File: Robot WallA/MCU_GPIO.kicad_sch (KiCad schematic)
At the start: 2 parts, among them J13 10129383-916001ALF, J6 10129383-916001ALF

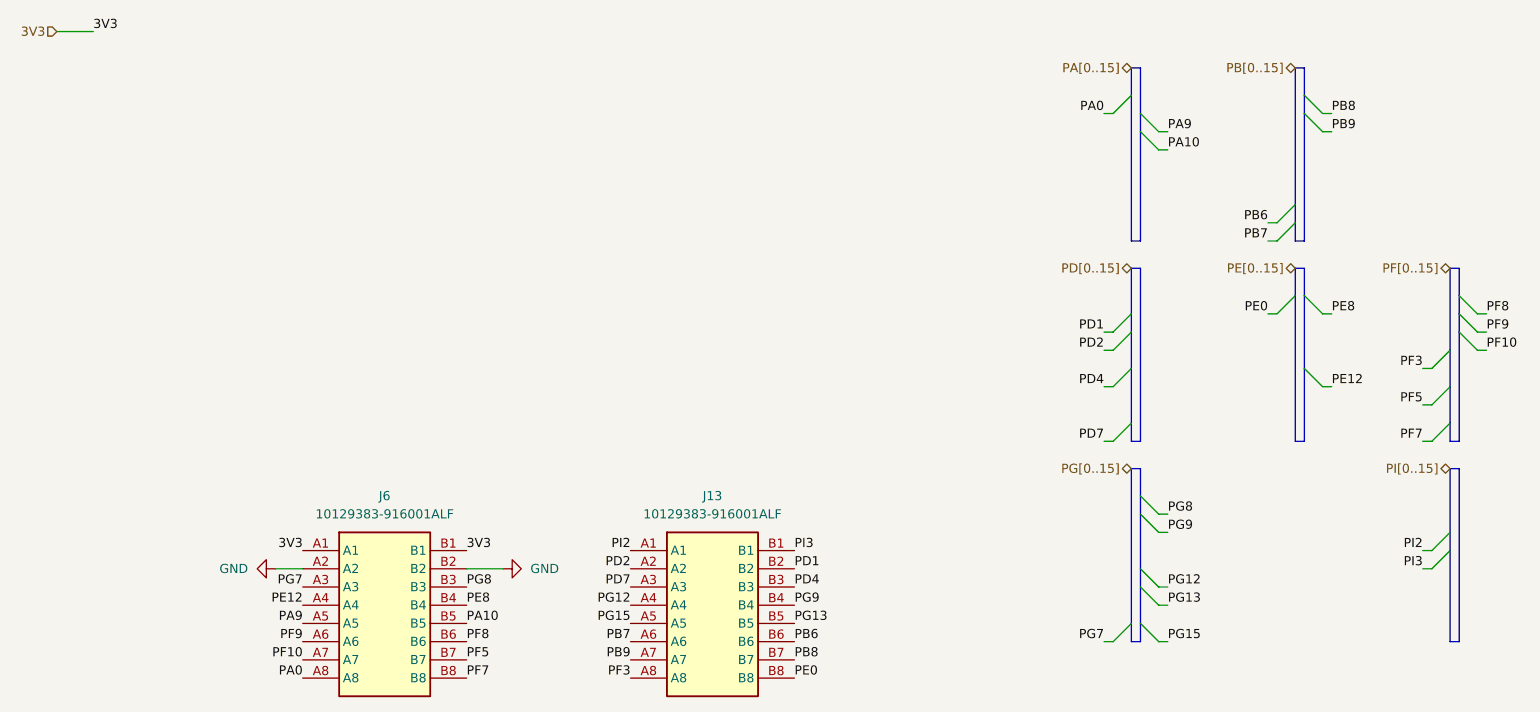
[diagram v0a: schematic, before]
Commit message: Modified a bit pin header pins to allow I2C,SPI and CAN
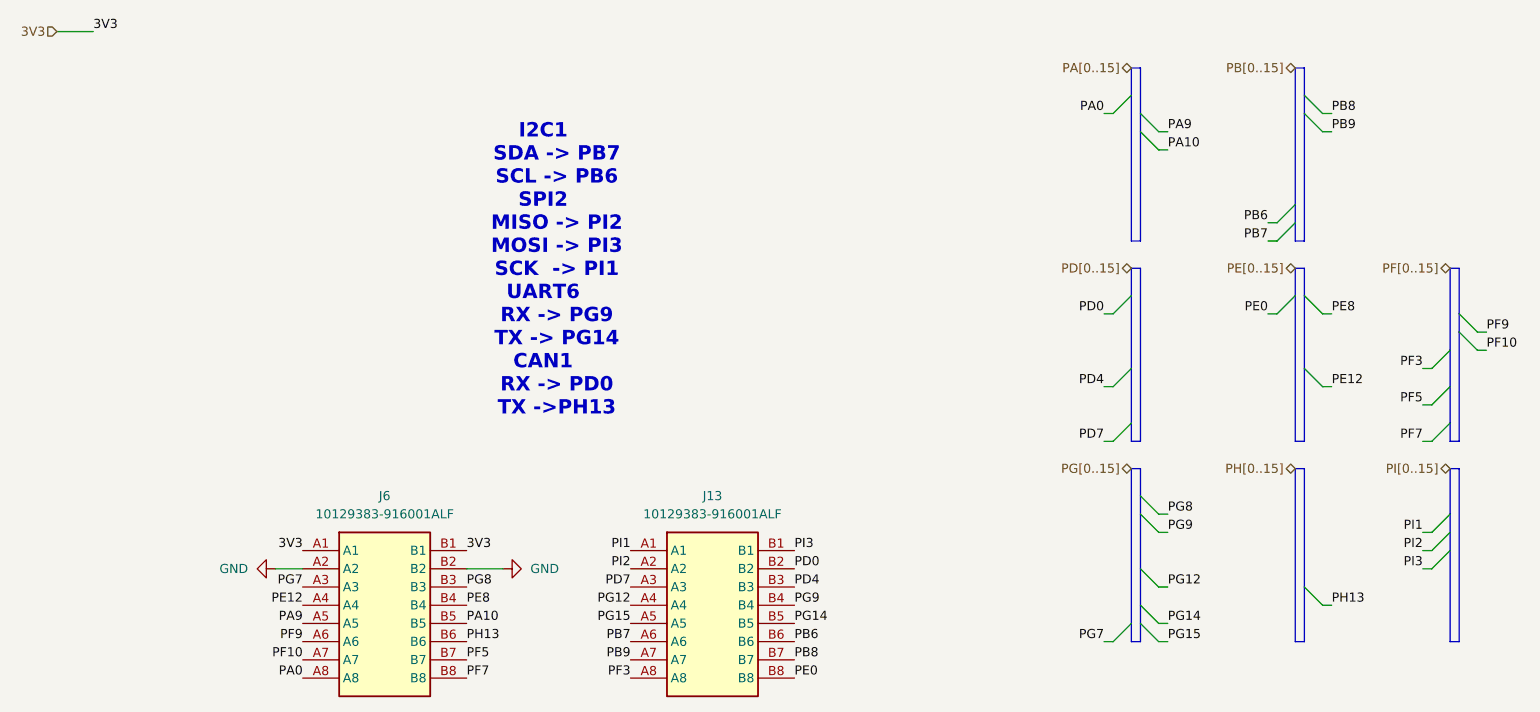
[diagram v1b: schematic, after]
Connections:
- net PD2 is gone; now on net PI2: J13.A2
- net PI2: no longer J13.A1
- net PD1 renamed PD0
- net PF8 renamed PH13
- net PG13 renamed PG14
- new net PI1: J13.A1
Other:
- note added: "I2C1 SDA -> PB7 SCL -> PB6 SPI2 MISO -> PI2 MOSI -> PI3 SCK -> PI1 UART6 RX -> PG9 TX -> PG14 CAN1 RX -> PD0 TX ->PH13"
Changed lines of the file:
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@@
 		(comment 2 "THO")
+	)
+	(text "I2C1\n	SDA -> PB7\n	SCL -> PB6\nSPI2\n	MISO -> PI2\n	MOSI -> PI3\n	SCK  -> PI1\nUART6\n	RX -> PG9\n	TX -> PG14\nCAN1\n	RX -> PD0\n	TX ->PH13"
+		(exclude_from_sim no)
+		(at 100.838 51.054 0)
+		(effects
+			(font
+				(size 2 2)
+				(thickness 0.4)
+				(bold yes)
+			)
+		)
 	)
 	(bus_entry
@@
 	)
 	(bus_entry
-		(at 182.88 57.15)
+		(at 182.88 54.61)
 		(size -2.54 2.54)
 		(stroke
@@
 	)
 	(bus_entry
-		(at 228.6 54.61)
-		(size 2.54 2.54)
-		(stroke
-			(width 0)
-			(type default)
-		)
-	)
-	(bus_entry
-		(at 184.15 95.25)
+		(at 184.15 97.79)
 		(size 2.54 2.54)
 		(stroke
@@
 	)
 	(bus_entry
+		(at 207.01 95.25)
+		(size 2.54 2.54)
+		(stroke
+			(width 0)
+			(type default)
+		)
+	)
+	(bus_entry
 		(at 205.74 41.91)
 		(size -2.54 2.54)
@@
 	)
 	(bus_entry
+		(at 227.33 85.09)
+		(size -2.54 2.54)
+		(stroke
+			(width 0)
+			(type default)
+		)
+	)
+	(bus_entry
 		(at 207.01 64.77)
 		(size 2.54 2.54)
@@
 	)
 	(bus_entry
-		(at 182.88 59.69)
-		(size -2.54 2.54)
-		(stroke
-			(width 0)
-			(type default)
-		)
-	)
-	(bus_entry
 		(at 227.33 90.17)
 		(size -2.54 2.54)
@@
 	(bus
 		(pts
+			(xy 205.74 78.74) (xy 205.74 102.87)
+		)
+		(stroke
+			(width 0)
+			(type default)
+		)
+	)
+	(bus
+		(pts
+			(xy 227.33 85.09) (xy 227.33 87.63)
+		)
+		(stroke
+			(width 0)
+			(type default)
+		)
+	)
+	(wire
+		(pts
+			(xy 209.55 97.79) (xy 210.82 97.79)
+		)
+		(stroke
+			(width 0)
+			(type default)
+		)
+	)
+	(bus
+		(pts
 			(xy 182.88 46.99) (xy 184.15 46.99)
 		)
@@
 	(bus
 		(pts
-			(xy 182.88 50.8) (xy 182.88 57.15)
+			(xy 182.88 50.8) (xy 182.88 54.61)
 		)
 		(stroke
@@
 	(bus
 		(pts
-			(xy 184.15 95.25) (xy 184.15 100.33)
+			(xy 184.15 92.71) (xy 184.15 97.79)
+		)
+		(stroke
+			(width 0)
+			(type default)
+		)
+	)
+	(bus
+		(pts
+			(xy 207.01 95.25) (xy 207.01 102.87)
 		)
 		(stroke
@@
 		)
 	)
-	(wire
-		(pts
-			(xy 179.07 62.23) (xy 180.34 62.23)
-		)
-		(stroke
-			(width 0)
-			(type default)
-		)
-	)
 	(bus
 		(pts
@@
 	(wire
 		(pts
-			(xy 231.14 57.15) (xy 232.41 57.15)
-		)
-		(stroke
-			(width 0)
-			(type default)
-		)
-	)
-	(wire
-		(pts
 			(xy 223.52 74.93) (xy 224.79 74.93)
 		)
@@
 	(bus
 		(pts
-			(xy 182.88 59.69) (xy 182.88 64.77)
-		)
-		(stroke
-			(width 0)
-			(type default)
-		)
-	)
-	(bus
-		(pts
-			(xy 227.33 78.74) (xy 227.33 87.63)
+			(xy 182.88 54.61) (xy 182.88 64.77)
+		)
+		(stroke
+			(width 0)
+			(type default)
+		)
+	)
+	(bus
+		(pts
+			(xy 227.33 78.74) (xy 227.33 85.09)
 		)
 		(stroke
@@
 	(bus
 		(pts
-			(xy 228.6 57.15) (xy 228.6 54.61)
-		)
-		(stroke
-			(width 0)
-			(type default)
-		)
-	)
-	(bus
-		(pts
 			(xy 184.15 85.09) (xy 184.15 92.71)
 		)
@@
 	(bus
 		(pts
+			(xy 207.01 78.74) (xy 205.74 78.74)
+		)
+		(stroke
+			(width 0)
+			(type default)
+		)
+	)
+	(bus
+		(pts
 			(xy 205.74 50.8) (xy 205.74 54.61)
 		)
@@
 	(bus
 		(pts
-			(xy 182.88 57.15) (xy 182.88 59.69)
-		)
-		(stroke
-			(width 0)
-			(type default)
-		)
-	)
-	(bus
-		(pts
 			(xy 228.6 78.74) (xy 227.33 78.74)
 		)
@@
 		)
 	)
-	(bus
-		(pts
-			(xy 184.15 95.25) (xy 184.15 92.71)
-		)
-		(stroke
-			(width 0)
-			(type default)
-		)
-	)
 	(wire
 		(pts
@@
 	(wire
 		(pts
-			(xy 179.07 59.69) (xy 180.34 59.69)
+			(xy 179.07 57.15) (xy 180.34 57.15)
+		)
+		(stroke
+			(width 0)
+			(type default)
+		)
+	)
+	(bus
+		(pts
+			(xy 205.74 102.87) (xy 207.01 102.87)
+		)
+		(stroke
+			(width 0)
+			(type default)
+		)
+	)
+	(wire
+		(pts
+			(xy 223.52 87.63) (xy 224.79 87.63)
 		)
 		(stroke
@@
 	(wire
 		(pts
-			(xy 186.69 97.79) (xy 187.96 97.79)
+			(xy 186.69 100.33) (xy 187.96 100.33)
 		)
 		(stroke
@@
 	(bus
 		(pts
-			(xy 228.6 54.61) (xy 228.6 50.8)
+			(xy 228.6 50.8) (xy 228.6 57.15)
 		)
 		(stroke
@@
 		(pts
 			(xy 207.01 50.8) (xy 205.74 50.8)
+		)
+		(stroke
+			(width 0)
+			(type default)
+		)
+	)
+	(bus
+		(pts
+			(xy 207.01 78.74) (xy 207.01 95.25)
+		)
+		(stroke
+			(width 0)
+			(type default)
+		)
+	)
+	(bus
+		(pts
+			(xy 184.15 97.79) (xy 184.15 100.33)
 		)
 		(stroke
@@
 		)
 	)
-	(label "PG13"
-		(at 187.96 97.79 0)
+	(label "PG14"
+		(at 187.96 100.33 0)
 		(effects
 			(font
@@
 		)
 	)
+	(label "PH13"
+		(at 210.82 97.79 0)
+		(effects
+			(font
+				(size 1.27 1.27)
+			)
+			(justify left bottom)
+		)
+	)
 	(label "PI2"
 		(at 223.52 90.17 180)
@@
 		)
 	)
-	(label "PD1"
-		(at 179.07 59.69 180)
-		(effects
-			(font
-				(size 1.27 1.27)
-			)
-			(justify right bottom)
+	(label "PD0"
+		(at 179.07 57.15 180)
+		(effects
+			(font
+				(size 1.27 1.27)
+			)
+			(justify right bottom)
+		)
+	)
+	(label "PH13"
+		(at 90.17 102.87 0)
+		(effects
+			(font
+				(size 1.27 1.27)
+			)
+			(justify left bottom)
 		)
 	)
@@
 		)
 	)
-	(label "PG13"
+	(label "PG14"
 		(at 135.89 100.33 0)
 		(effects
@@
 		)
 	)
-	(label "PD2"
-		(at 113.03 92.71 180)
+	(label "PI1"
+		(at 113.03 90.17 180)
 		(effects
 			(font
@@
 	)
 	(label "PI2"
-		(at 113.03 90.17 180)
+		(at 113.03 92.71 180)
 		(effects
 			(font
@@
 		)
 	)
-	(label "PF8"
-		(at 232.41 57.15 0)
-		(effects
-			(font
-				(size 1.27 1.27)
-			)
-			(justify left bottom)
-		)
-	)
 	(label "PI3"
 		(at 223.52 92.71 180)
@@
 		)
 	)
-	(label "PF8"
-		(at 90.17 102.87 0)
-		(effects
-			(font
-				(size 1.27 1.27)
-			)
-			(justify left bottom)
-		)
-	)
 	(label "PE8"
 		(at 90.17 97.79 0)
@@
 		)
 	)
+	(label "PI1"
+		(at 223.52 87.63 180)
+		(effects
+			(font
+				(size 1.27 1.27)
+			)
+			(justify right bottom)
+		)
+	)
 	(label "PG12"
 		(at 187.96 95.25 0)
@@
 		)
 	)
-	(label "PD2"
-		(at 179.07 62.23 180)
-		(effects
-			(font
-				(size 1.27 1.27)
-			)
-			(justify right bottom)
-		)
-	)
-	(label "PD1"
+	(label "PD0"
 		(at 135.89 92.71 0)
 		(effects
@@
 		(effects
 			(font
+				(size 1.27 1.27)
+			)
+			(justify right)
+		)
+	)
+	(hierarchical_label "PH[0..15]"
+		(shape bidirectional)
+		(at 205.74 78.74 180)
+		(effects
+			(font

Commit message: Updated Fab files
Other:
- note added: "DEBUG UART RX -> PA10 TX -> PA9 I2C1 SDA -> PB7 SCL -> PB6 SPI2 MISO -> PI2 MOSI -> PI3 SCK -> PI1 UART6 RX -> PG9 TX -> PG14 CAN1 RX -> PD0 TX ->PH13"
- note removed: "I2C1 SDA -> PB7 SCL -> PB6 SPI2 MISO -> PI2 MOSI -> PI3 SCK -> PI1 UART6 RX -> PG9 TX -> PG14 CAN1 RX -> PD0 TX ->PH13"
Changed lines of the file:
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@@
 		(comment 2 "THO")
 	)
-	(text "I2C1\n	SDA -> PB7\n	SCL -> PB6\nSPI2\n	MISO -> PI2\n	MOSI -> PI3\n	SCK  -> PI1\nUART6\n	RX -> PG9\n	TX -> PG14\nCAN1\n	RX -> PD0\n	TX ->PH13"
+	(text "DEBUG UART\n	RX -> PA10\n	TX -> PA9\nI2C1\n	SDA -> PB7\n	SCL -> PB6\nSPI2\n	MISO -> PI2\n	MOSI -> PI3\n	SCK  -> PI1\nUART6\n	RX -> PG9\n	TX -> PG14\nCAN1\n	RX -> PD0\n	TX ->PH13"
 		(exclude_from_sim no)
 		(at 100.838 51.054 0)

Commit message: Added 3 thermistor to measure temperature near 12V and 24V power supplies and near motor drivers
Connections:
- net PF7 is gone; now on net PF5: J6.B8
- net PF5: no longer J6.B7
- new net PF4: J6.B7
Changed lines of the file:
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@@
 	)
 	(bus_entry
-		(at 227.33 72.39)
+		(at 227.33 64.77)
 		(size -2.54 2.54)
 		(stroke
@@
 		)
 	)
+	(bus
+		(pts
+			(xy 227.33 64.77) (xy 227.33 67.31)
+		)
+		(stroke
+			(width 0)
+			(type default)
+		)
+	)
 	(wire
 		(pts
@@
 	(wire
 		(pts
-			(xy 223.52 74.93) (xy 224.79 74.93)
+			(xy 223.52 67.31) (xy 224.79 67.31)
 		)
 		(stroke
@@
 	(bus
 		(pts
-			(xy 227.33 72.39) (xy 227.33 74.93)
+			(xy 227.33 67.31) (xy 227.33 74.93)
 		)
 		(stroke
@@
 	(bus
 		(pts
-			(xy 227.33 67.31) (xy 227.33 72.39)
-		)
-		(stroke
-			(width 0)
-			(type default)
-		)
-	)
-	(bus
-		(pts
 			(xy 184.15 85.09) (xy 184.15 92.71)
 		)
@@
 	(bus
 		(pts
-			(xy 227.33 62.23) (xy 227.33 67.31)
+			(xy 227.33 62.23) (xy 227.33 64.77)
 		)
 		(stroke
@@
 		)
 	)
-	(label "PF7"
-		(at 223.52 74.93 180)
+	(label "PF4"
+		(at 223.52 67.31 180)
 		(effects
 			(font
@@
 		)
 	)
+	(label "PF4"
+		(at 90.17 105.41 0)
+		(effects
+			(font
+				(size 1.27 1.27)
+			)
+			(justify left bottom)
+		)
+	)
 	(label "PG14"
 		(at 135.89 100.33 0)
@@
 	)
 	(label "PF5"
-		(at 90.17 105.41 0)
+		(at 90.17 107.95 0)
 		(effects
 			(font
@@
 		(effects
 			(font
-				(size 1.27 1.27)
-			)
-			(justify left bottom)
-		)
-	)
-	(label "PF7"
-		(at 90.17 107.95 0)
-		(effects
-			(font
